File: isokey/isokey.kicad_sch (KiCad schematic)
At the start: 75 parts, among them Q1 BSS138, U1 BlackPill_STLINK, U3 TLV73318PDBV

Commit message: Continue routing
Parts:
- removed R17 (x14): 22R, Resistor_SMD:R_0603_1608Metric_Pad0.98x0.95mm_HandSolder, symbol Device:R
- added R17 (x16): 22R, Resistor_SMD:R_0603_1608Metric_Pad0.98x0.95mm_HandSolder, symbol Device:R
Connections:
- net sw1_r is gone; now on net sw0_r: RSW1.S2
- net +3.3V: no longer U1.41 (3.3V)
- net ENC1A: now also R17.2
- net ENC1B: now also R17.2
- net cl0: now also R17.1, R17.1, RSW1.S1
- net cl1: now also R17.1, R17.1
- net cl2: now also R17.1, R17.1
- net cl3: now also R17.1, R17.1; no longer R17.2
- net cl4: now also R17.1, R17.1; no longer R17.2
- net cl5: now also R17.1, R17.1
- net cl6: now also R17.1, R17.1; no longer RSW1.S1
- net cl7: now also R17.1, R17.1
- net cl8: now also R17.1, R17.1
- net cl9: now also R17.1, R17.1
- net r0: now also R17.1, R17.1
- net r1: now also R17.1, R17.1
- net r2: now also R17.1, R17.1
- net r3: now also R17.1, R17.1
- net r4: now also R17.1, R17.1
- net at R17.2: no longer U1.9 (PA12)
- net at R17.2: no longer U1.26 (PA0)
- net at R17.2: no longer U1.7 (PA10)
- net at R17.2: no longer U1.30 (PA4)
- net at R17.2: no longer U1.32 (PA6)
- net at R17.2: no longer U1.5 (PA8)
- net at R17.2: no longer U1.31 (PA5)
- net at R17.2: no longer U1.8 (PA11)
- net at R17.2: no longer U1.10 (PA15)
- net at R17.2: no longer U1.33 (PA7)
- net at R17.2: no longer U1.28 (PA2)
- net at R17.2: no longer U1.27 (PA1)
- net at U1.29 (PA3): no longer R17.2
- net at U1.6 (PA9): no longer R17.2
- net PA13: no longer names the net of U1.42 (SWDIO)
- net PA14: no longer names the net of U1.43 (SWSCK)
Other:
- sheet keyplate ports: added none; removed sw1_r
- moved on the sheet: C13, R17

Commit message: Continue routing
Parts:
- removed C13 (x4): 1uF, Capacitor_SMD:C_0805_2012Metric, symbol Device:C
- removed C13 (x3): 100nF, Capacitor_SMD:C_0603_1608Metric_Pad1.08x0.95mm_HandSolder, symbol Device:C
- removed Q1: BSS138, Package_TO_SOT_SMD:SOT-23-3, symbol Simulation_SPICE:NMOS
- removed R17 (x4): 22R, Resistor_SMD:R_0603_1608Metric_Pad0.98x0.95mm_HandSolder, symbol Device:R
- removed R17: 4k7, Resistor_SMD:R_0603_1608Metric_Pad0.98x0.95mm_HandSolder, symbol Device:R
- removed R17, R25, R26 (x3), R27: 10k, Resistor_SMD:R_0603_1608Metric_Pad0.98x0.95mm_HandSolder, symbol Device:R
- removed RSW1: RotaryEncoder_Switch, Rotary_Encoder:RotaryEncoder_Alps_EC12E-Switch_Vertical_H20mm_CircularMountingHoles, symbol Device:RotaryEncoder_Switch
- removed U2: ~, Display:OLED_Display_128x32_SSD1306_i2c, symbol Display_Graphic:OLED_Display_128x32_SSD1306_i2c
- removed U3: TLV73318PDBV, Package_TO_SOT_SMD:SOT-23-5, symbol Regulator_Linear:TLV73318PDBV
- added C13 (x4): 10uF, Capacitor_SMD:C_1206_3216Metric, symbol Device:C
- added C13 (x2): 1uF, Capacitor_SMD:C_0805_2012Metric, symbol Device:C
- added JP1, JP10, JP11, JP12, JP13, JP14, JP15, JP16, JP17, JP18, JP19, JP2, JP20, JP21, JP22, JP23, JP24, JP25, JP26, JP27, JP28, JP29, JP3, JP30, JP31, JP32, JP33, JP34, JP35, JP36, JP37, JP38, JP39, JP4, JP40, JP5, JP6, JP7, JP8, JP9: SolderJumper_3_Open_line, Jumper:SolderJumper-3_P2.0mm_Open_TrianglePad1.0x1.5mm_NumberLabels, symbol Jumper:SolderJumper_3_Open_line
- added Q2, Q3: BSS138, Package_TO_SOT_SMD:SOT-23-3, symbol Simulation_SPICE:NMOS
- added R17 (x11): 22R, Resistor_SMD:R_0603_1608Metric_Pad0.98x0.95mm_HandSolder, symbol Device:R
- added R17 (x2): 4k7, Resistor_SMD:R_0603_1608Metric_Pad0.98x0.95mm_HandSolder, symbol Device:R
- added R17 (x2): 10k, Resistor_SMD:R_0603_1608Metric_Pad0.98x0.95mm_HandSolder, symbol Device:R
- U1: footprint Module:BlackPill_doble_top-bot -> Module:BlackPill
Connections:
- net cl10 is gone; now on net cl9: TP7.1
- net +3.3V: now also C13.1, C13.1, JP20.3 (B), JP21.1 (A), JP3.1 (A), JP38.3 (B), Q2.2 (G), Q3.2 (G), R17.2, R17.2; no longer U1.20 (3V3), U1.38 (3V3)
- net +5V: now also C13.1, C13.1, C13.1, C13.1, JP18.3 (B), JP2.1 (A), JP23.1 (A), JP40.1 (A), R17.2, R17.2; no longer U1.18 (5V), U1.40 (5V)
- net ENC1A: now also R17.1, R17.1
- net ENC1B: now also R17.1, R17.1
- net GND: now also C13.2, C13.2, C13.2, C13.2, C13.2, C13.2, JP1.1 (A), JP19.3 (B), JP22.1 (A), JP39.3 (B); no longer U1.19 (GND), U1.39 (GND), U1.44 (GND)
- net cl5: now also TP1.1
- net cl6: now also TP2.1; no longer TP1.1
- net cl7: now also TP3.1; no longer TP2.1
- net cl8: now also TP4.1; no longer TP3.1
- net cl9: no longer TP4.1
- net led_SCL: now also R17.1, R17.1
- net led_SDA: now also R17.1, R17.1
- net led_w1: now also R17.1, Q2.3 (S), Q3.3 (S), R17.1, R17.1, R17.1; no longer R17.2
- net led_w1_in: now also Q2.1 (D), Q3.1 (D), R17.1, R17.1
- net led_w1_out: now also R17.2
- net pc15: now reaches R17.2
- net pc15: now also R17.2, JP17.1 (A), JP24.3 (B)
- net at R17.1, TP8.1: now also R17.1
- net pa8: now reaches R17.2
- net pa8: now also R17.2, JP36.1 (A), JP5.3 (B)
- net pb14: now reaches R17.2
- net pb14: now also R17.2, JP3.3 (B), JP38.1 (A)
- net 2: now reaches U1.2 (PB13)
- net 2: now also JP1.2 (C)
- net pb0: now reaches R17.2
- net pb0: now also R17.2, JP34.3 (B), JP7.1 (A)
- net pb2: now reaches R17.2
- net pb2: now also R17.2, JP36.3 (B), JP5.1 (A)
- net pa1: now reaches R17.2
- net pa1: now also R17.2, JP14.1 (A), JP27.3 (B)
- net pb15: now reaches R17.2
- net pb15: now also R17.2, JP37.1 (A), JP4.3 (B)
- net 14: now reaches U1.14 (PB6)
- net 14: now also JP14.2 (C)
- net pb8: now reaches R17.2
- net pb8: now also R17.2, JP16.3 (B), JP25.1 (A)
- net 15: now reaches U1.15 (PB7)
- net 15: now also JP15.2 (C)
- net pb4: now reaches R17.2
- net pb4: now also R17.2, JP12.3 (B), JP29.1 (A)
- net pb5: now reaches R17.2
- net pb5: now also R17.2, JP13.3 (B), JP28.1 (A)
- net pa2: now reaches R17.2
- net pa2: now also R17.2, JP13.1 (A), JP28.3 (B)
- net pc13: now reaches R17.2
- net pc13: now also R17.2, JP19.1 (A), JP22.3 (B)
- net at R17.1, TP11.1: now also R17.1
- net 11: now reaches U1.11 (PB3)
- net 11: now also JP11.2 (C); no longer R17.1
- net pa0: now reaches R17.2
- net pa0: now also R17.2, JP15.1 (A), JP26.3 (B)
- net pb10: now reaches R17.2
- net pb10: now also R17.2, JP37.3 (B), JP4.1 (A)
- net pa3: now reaches R17.2
- net pa3: now also R17.2, JP12.1 (A), JP29.3 (B)
- net 1: now reaches U1.1 (PB12)
- net 1: now also JP2.2 (C)
- net 10: now reaches U1.10 (PA15)
- net 10: now also JP10.2 (C)
- net 12: now reaches U1.12 (PB4)
- net 12: now also JP12.2 (C)
- net 13: now reaches U1.13 (PB5)
- net 13: now also JP13.2 (C)
- net 16: now reaches U1.16 (PB8)
- net 16: now also JP16.2 (C)
- net 17: now reaches U1.17 (PB9)
- net 17: now also JP17.2 (C)
- net 21: now reaches U1.21 (VBAT)
- net 21: now also JP21.2 (C)
- net 22: now reaches U1.22 (PC13)
- net 22: now also JP22.2 (C)
- net 23: now reaches U1.23 (PC14)
- net 23: now also JP23.2 (C)
- net 24: now reaches U1.24 (PC15)
- net 24: now also JP24.2 (C)
- net 25: now reaches U1.25 (~{RESET})
- net 25: now also JP25.2 (C)
- net 26: now reaches U1.26 (PA0)
- net 26: now also JP26.2 (C)
- net 27: now reaches U1.27 (PA1)
- net 27: now also JP27.2 (C)
- net 28: now reaches U1.28 (PA2)
- net 28: now also JP28.2 (C)
- net 29: now reaches U1.29 (PA3)
- net 29: now also JP29.2 (C)
- net 3: now reaches U1.3 (PB14)
- net 3: now also JP3.2 (C)
- net 30: now reaches U1.30 (PA4)
- net 30: now also JP30.2 (C)
- net 31: now reaches U1.31 (PA5)
- net 31: now also JP31.2 (C)
- net 32: now reaches U1.32 (PA6)
- net 32: now also JP32.2 (C)
- net 33: now reaches U1.33 (PA7)
- net 33: now also JP33.2 (C)
- net 34: now reaches U1.34 (PB0)
- net 34: now also JP34.2 (C)
- net 35: now reaches U1.35 (PB1)
- net 35: now also JP35.2 (C)
- net 37: now reaches U1.37 (PB10)
- net 37: now also JP37.2 (C)
- net 4: now reaches U1.4 (PB15)
- net 4: now also JP4.2 (C)
- net 5: now reaches U1.5 (PA8)
- net 5: now also JP5.2 (C)
- net 6: now reaches U1.6 (PA9)
- net 6: now also JP6.2 (C)
- net 7: now reaches U1.7 (PA10)
- net 7: now also JP7.2 (C)
- net 8: now reaches U1.8 (PA11)
- net 8: now also JP8.2 (C)
- net 9: now reaches U1.9 (PA12)
- net 9: now also JP9.2 (C)
- net port_id renamed 36
- net 36: now also JP36.2 (C); no longer R17.2
- new net 18: JP18.2 (C), U1.18 (5V)
- new net 19: JP19.2 (C), U1.19 (GND)
- new net 20: JP20.2 (C), U1.20 (3V3)
- new net 38: JP38.2 (C), U1.38 (3V3)
- new net 39: JP39.2 (C), U1.39 (GND)
- new net 40: JP40.2 (C), U1.40 (5V)
- new net V_BATT: JP20.1 (A), JP21.3 (B)
- new net pa10: JP34.1 (A), JP7.3 (B)
- new net pa11: JP33.1 (A), JP8.3 (B)
- new net pa12: JP32.1 (A), JP9.3 (B)
- new net pa15: JP10.3 (B), JP31.1 (A)
- new net pa4: JP11.1 (A), JP30.3 (B)
- new net pa5: JP10.1 (A), JP31.3 (B)
- new net pa6: JP32.3 (B), JP9.1 (A)
- new net pa7: JP33.3 (B), JP8.1 (A)
- new net pa9: JP35.1 (A), JP6.3 (B)
- new net pb1: JP35.3 (B), JP6.1 (A)
- new net pb12: JP2.3 (B), JP40.3 (B), R17.2, R17.2
- new net pb13: JP1.3 (B), JP39.1 (A), R17.2, R17.2
- new net pb3: JP11.3 (B), JP30.1 (A), R17.2, R17.2
- new net pb6: JP14.3 (B), JP27.1 (A), R17.2, R17.2
- new net pb7: JP15.3 (B), JP26.1 (A), R17.2, R17.2
- new net pb9: JP17.3 (B), JP24.1 (A)
- new net pc14: JP18.1 (A), JP23.3 (B), R17.2, R17.2
- new net reset: JP16.1 (A), JP25.3 (B)
- no-connect marks 3 -> 4
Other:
- added sheet Interfaces (interfaces.kicad_sch)
- moved on the sheet: H1, H2, H3, H4, R17, TP1, TP10, TP11, TP2, TP3, TP4, TP5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

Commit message: Complete routing
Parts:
- removed H1, H2, H3: StabilizerHoles, Button_Switch_Keyboard:Stabilizer_MX_2u, symbol Mechanical:MountingHole
- added J1, J2: PJ-320A-4P, Connector_Audio:Jack_3.5mm_PJ320E_Horizontal, symbol Connector_Audio:AudioJack4_Ground
- added JP47, JP48, JP49, JP50: SolderJumper_3_Open_line, Jumper:SolderJumper-3_P2.0mm_Open_TrianglePad1.0x1.5mm_NumberLabels, symbol Jumper:SolderJumper_3_Open_line
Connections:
- net +5V: now also JP49.3 (B), JP50.3 (B)
- net GND: now also J1.G, J2.G, JP49.2 (C), JP50.2 (C)
- net Led_INT: now also JP47.3 (B)
- net pa2: now also JP47.2 (C), JP48.2 (C); no longer R17.2, R17.2
- net pa3: now also JP48.3 (B); no longer R17.2, R17.2
- net pa6: now also R17.2, R17.2
- net pa7: now also R17.2, R17.2
- new net: J1.T, J2.S, JP50.1 (A)
- new net: J1.S, J2.T, JP49.1 (A)
- new net: J1.R1, J2.R1, JP47.1 (A)
- new net: J1.R2, J2.R2, JP48.1 (A)
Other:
- note added: "Rx"
- note added: "Tx"

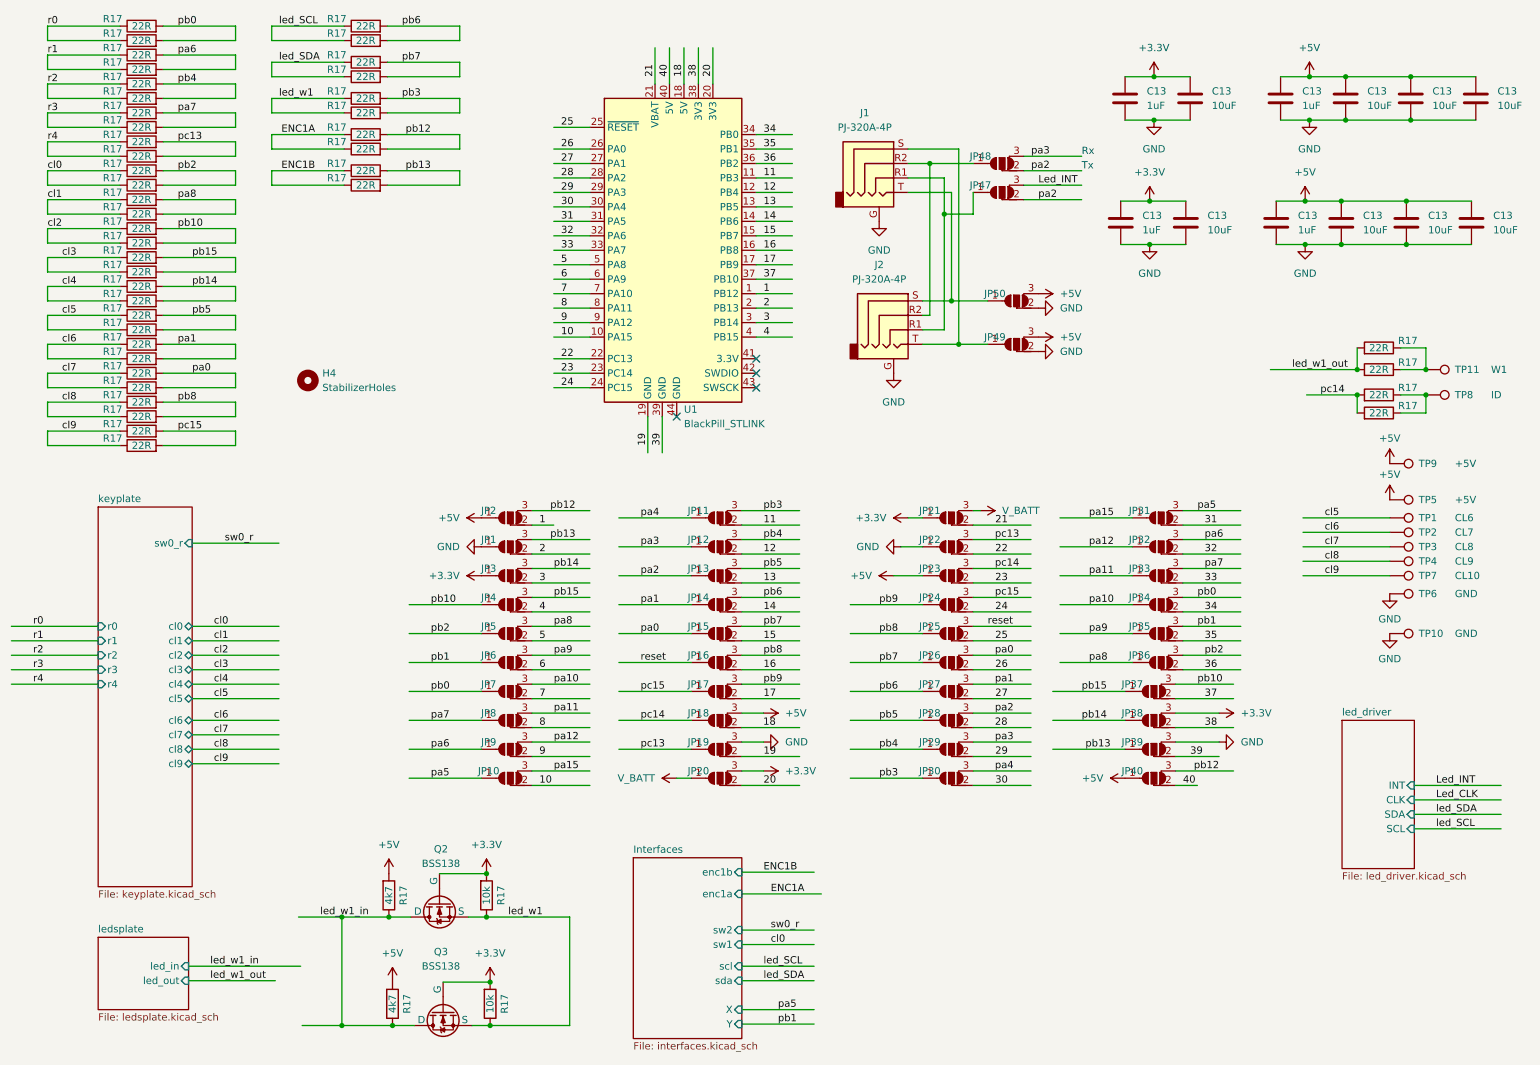
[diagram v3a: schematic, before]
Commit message: Reoder prj. Complete routing fix drc.
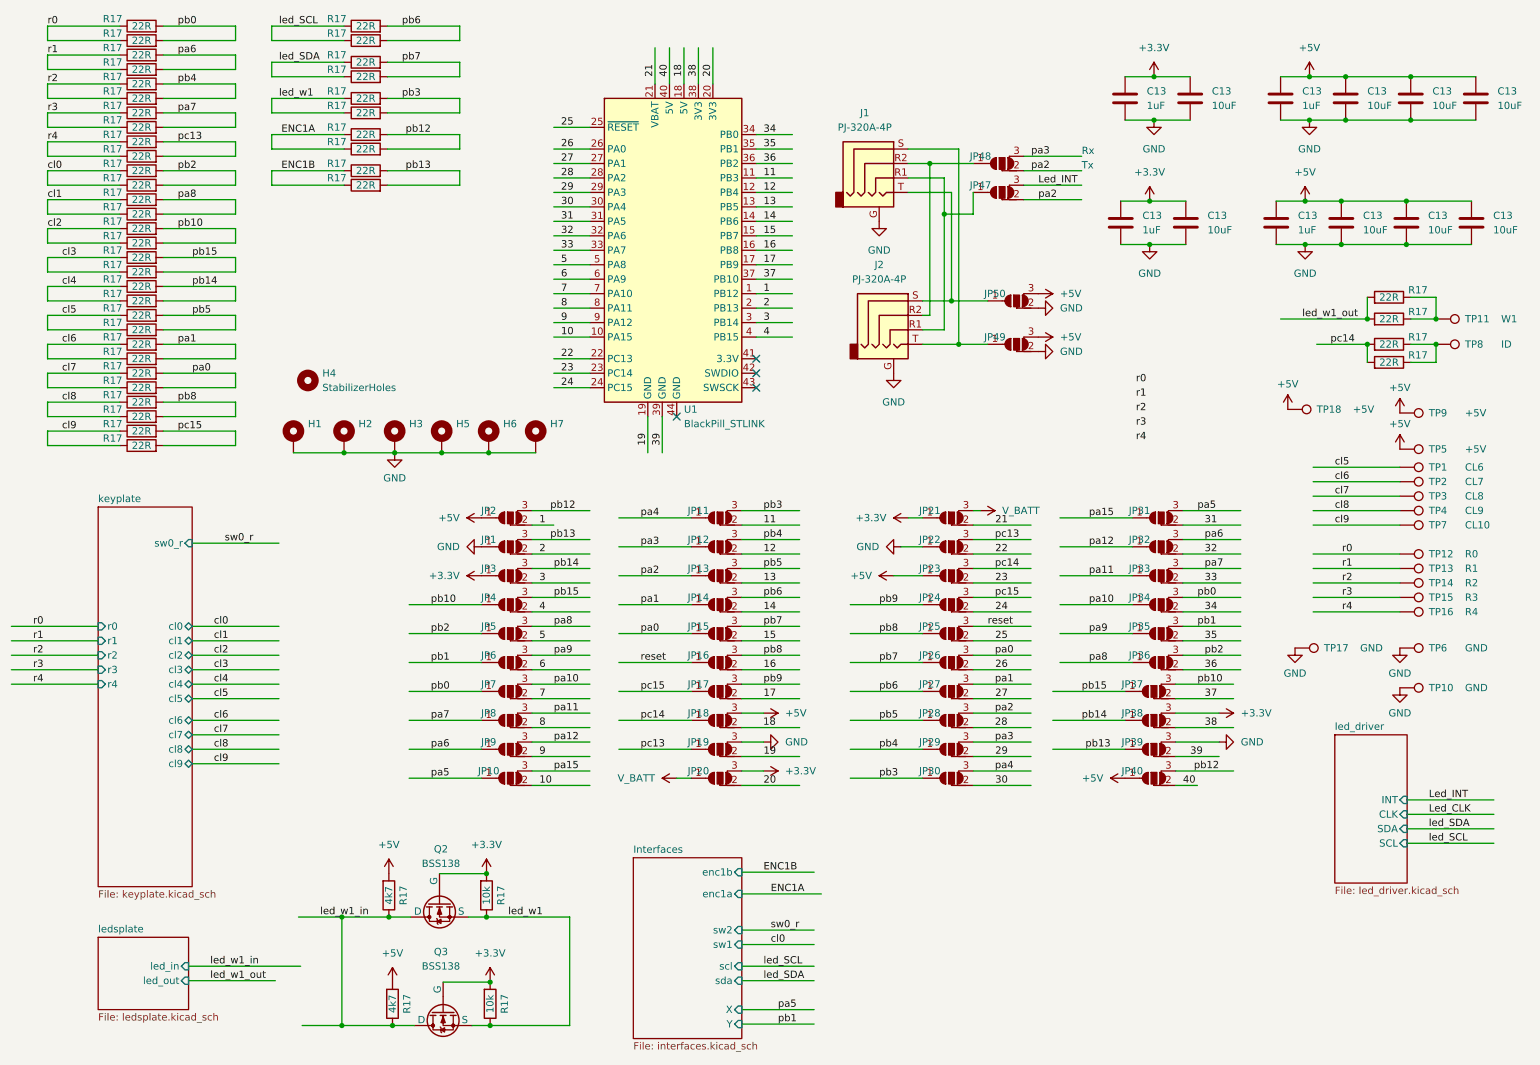
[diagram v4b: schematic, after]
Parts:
- added H1, H2, H3, H5, H6, H7: MountingHole_Pad, MountingHole:MountingHole_2.5mm_Pad_TopBottom, symbol Mechanical:MountingHole_Pad
- added TP12: R0, TestPoint:Testpoint_Pad_1.0x2.0mm, symbol Connector:TestPoint
- added TP13: R1, TestPoint:Testpoint_Pad_1.0x2.0mm, symbol Connector:TestPoint
- added TP14: R2, TestPoint:Testpoint_Pad_1.0x2.0mm, symbol Connector:TestPoint
- added TP15: R3, TestPoint:Testpoint_Pad_1.0x2.0mm, symbol Connector:TestPoint
- added TP16: R4, TestPoint:Testpoint_Pad_1.0x2.0mm, symbol Connector:TestPoint
- added TP17: GND, TestPoint:Testpoint_Pad_1.0x2.0mm, symbol Connector:TestPoint
- added TP18: +5V, TestPoint:Testpoint_Pad_1.0x2.0mm, symbol Connector:TestPoint
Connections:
- net +5V: now also TP18.1
- net GND: now also H1.1, H2.1, H3.1, H5.1, H6.1, H7.1, TP17.1
- net r0: now also TP12.1
- net r1: now also TP13.1
- net r2: now also TP14.1
- net r3: now also TP15.1
- net r4: now also TP16.1
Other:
- moved on the sheet: R17, TP1, TP10, TP11, TP2, TP3, TP4, TP5, TP6, TP7, TP8, TP9
